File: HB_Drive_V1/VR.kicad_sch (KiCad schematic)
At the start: 0 parts

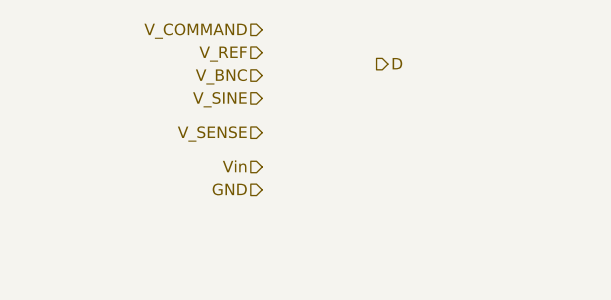
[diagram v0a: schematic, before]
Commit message: fixes git and adds a first revision of the Inner Current Regulator (NOT COMPLETE)
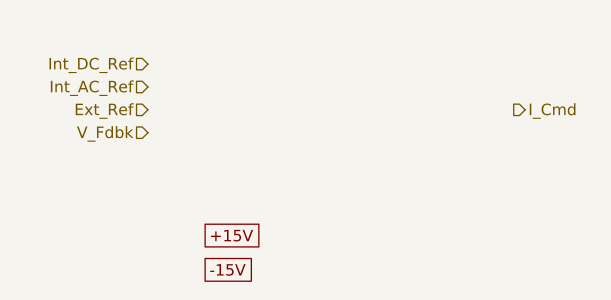
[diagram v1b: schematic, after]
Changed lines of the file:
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@@
 	(generator_version "10.0")
 	(paper "A4")
-	(hierarchical_label "V_REF"
+	(global_label "+15V"
+		(shape passive)
+		(at 120.65 86.36 0)
+		(fields_autoplaced yes)
+		(effects
+			(font
+				(size 1.27 1.27)
+			)
+			(justify left)
+		)
+		(property "Intersheetrefs" "${INTERSHEET_REFS}"
+			(at 127.6039 86.36 0)
+			(hide yes)
+			(show_name no)
+			(do_not_autoplace no)
+			(effects
+				(font
+					(size 1.27 1.27)
+				)
+				(justify left)
+			)
+		)
+	)
+	(global_label "-15V"
+		(shape passive)
+		(at 120.65 90.17 0)
+		(fields_autoplaced yes)
+		(effects
+			(font
+				(size 1.27 1.27)
+			)
+			(justify left)
+		)
+		(property "Intersheetrefs" "${INTERSHEET_REFS}"
+			(at 127.6039 90.17 0)
+			(hide yes)
+			(show_name no)
+			(do_not_autoplace no)
+			(effects
+				(font
+					(size 1.27 1.27)
+				)
+				(justify left)
+			)
+		)
+	)
+	(hierarchical_label "Int_AC_Ref"
 		(shape input)
-		(at 127 66.04 180)
+		(at 114.3 69.85 180)
 		(effects
 			(font
@@
 		)
 	)
-	(hierarchical_label "Vin"
+	(hierarchical_label "I_Cmd"
+		(shape output)
+		(at 154.94 72.39 0)
+		(effects
+			(font
+				(size 1.27 1.27)
+			)
+			(justify left)
+		)
+	)
+	(hierarchical_label "Ext_Ref"
 		(shape input)
-		(at 127 78.74 180)
+		(at 114.3 72.39 180)
 		(effects
 			(font
@@
 		)
 	)
-	(hierarchical_label "V_SINE"
+	(hierarchical_label "V_Fdbk"
 		(shape input)
-		(at 127 71.12 180)
+		(at 114.3 74.93 180)
 		(effects
 			(font
@@
 		)
 	)
-	(hierarchical_label "D"
-		(shape output)
-		(at 139.7 67.31 0)
+	(hierarchical_label "Int_DC_Ref"
+		(shape input)
+		(at 114.3 67.31 180)
 		(effects
 			(font
-				(size 1.27 1.27)
-			)
-			(justify left)
-		)
-	)
-	(hierarchical_label "V_BNC"
-		(shape input)
-		(at 127 68.58 180)
-		(effects
-			(font
-				(size 1.27 1.27)
-			)
-			(justify right)
-		)
-	)
-	(hierarchical_label "V_SENSE"
-		(shape input)
-		(at 127 74.93 180)
-		(effects
-			(font
-				(size 1.27 1.27)
-			)
-			(justify right)
-		)
-	)
-	(hierarchical_label "V_COMMAND"
-		(shape input)
-		(at 127 63.5 180)
-		(effects
-			(font
-				(size 1.27 1.27)
-			)
-			(justify right)
-		)
-	)
-	(hierarchical_label "GND"
-		(shape input)
-		(at 127 81.28 180)
-		(effects
-			(font

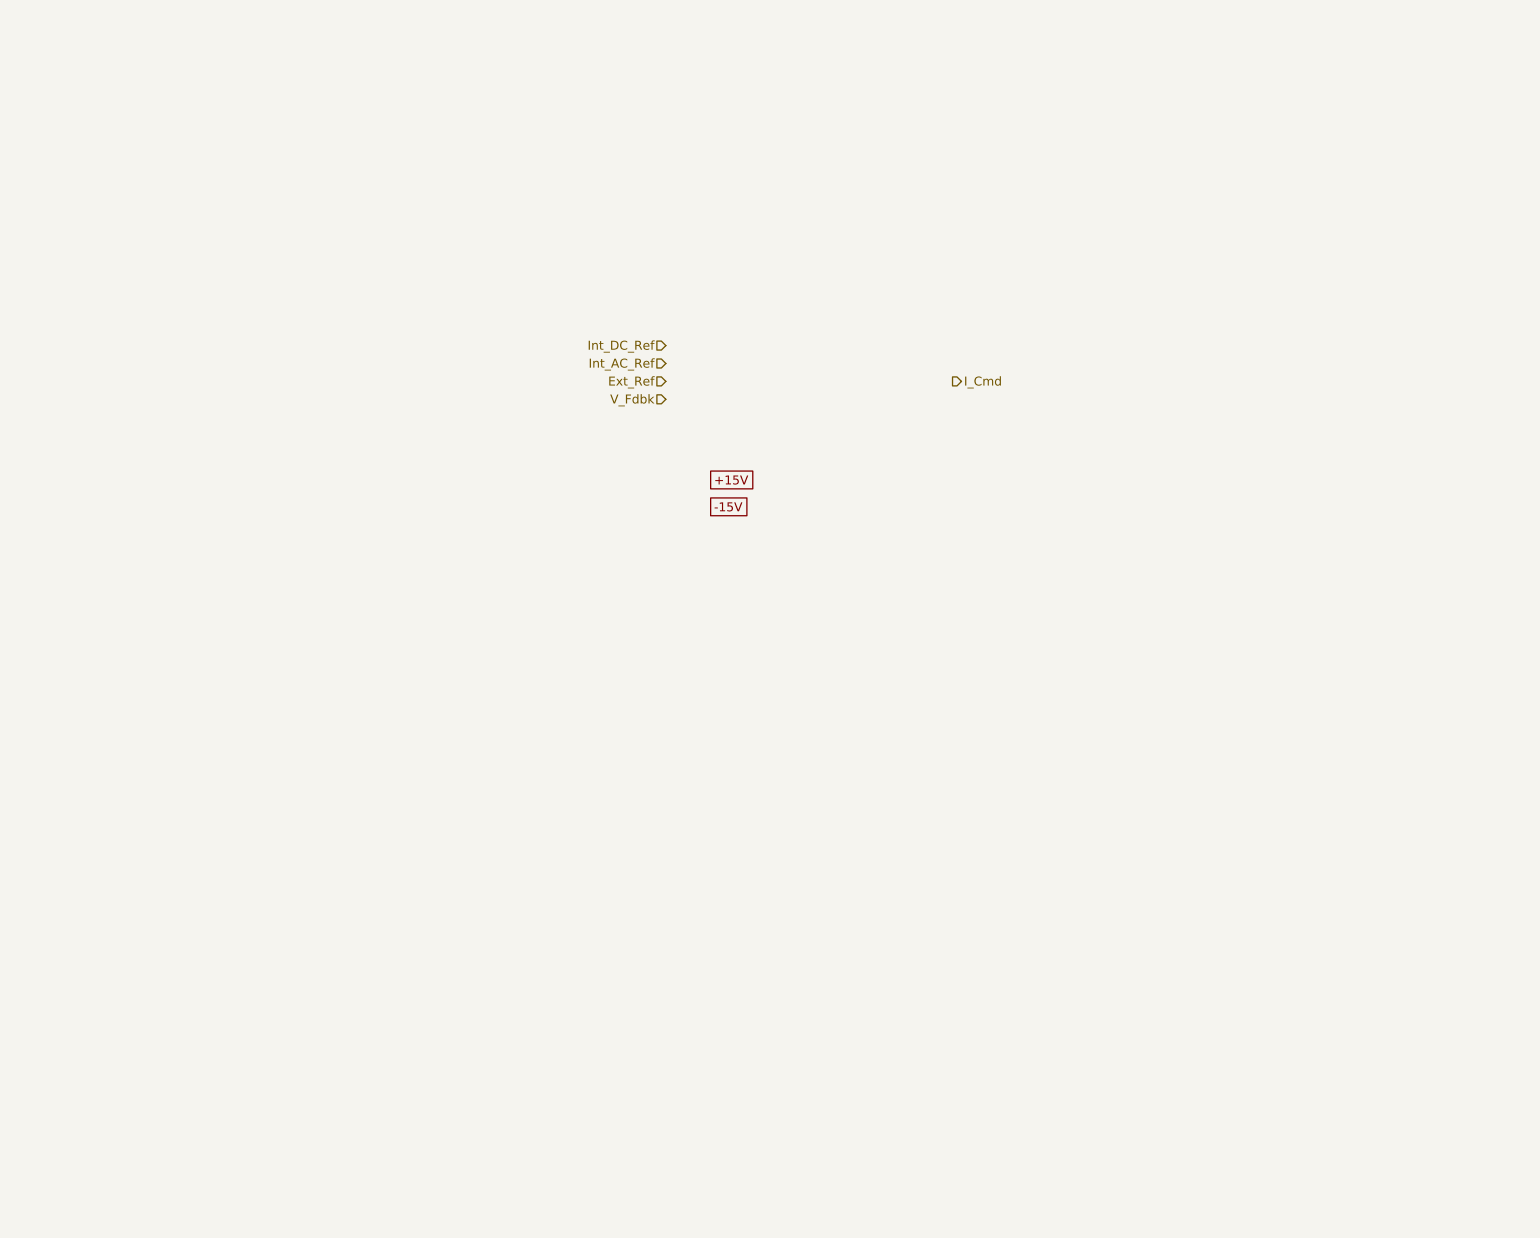
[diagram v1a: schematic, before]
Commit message: adds 10v reference and DC offsets / gain control to I_fdbk and V_fdbk
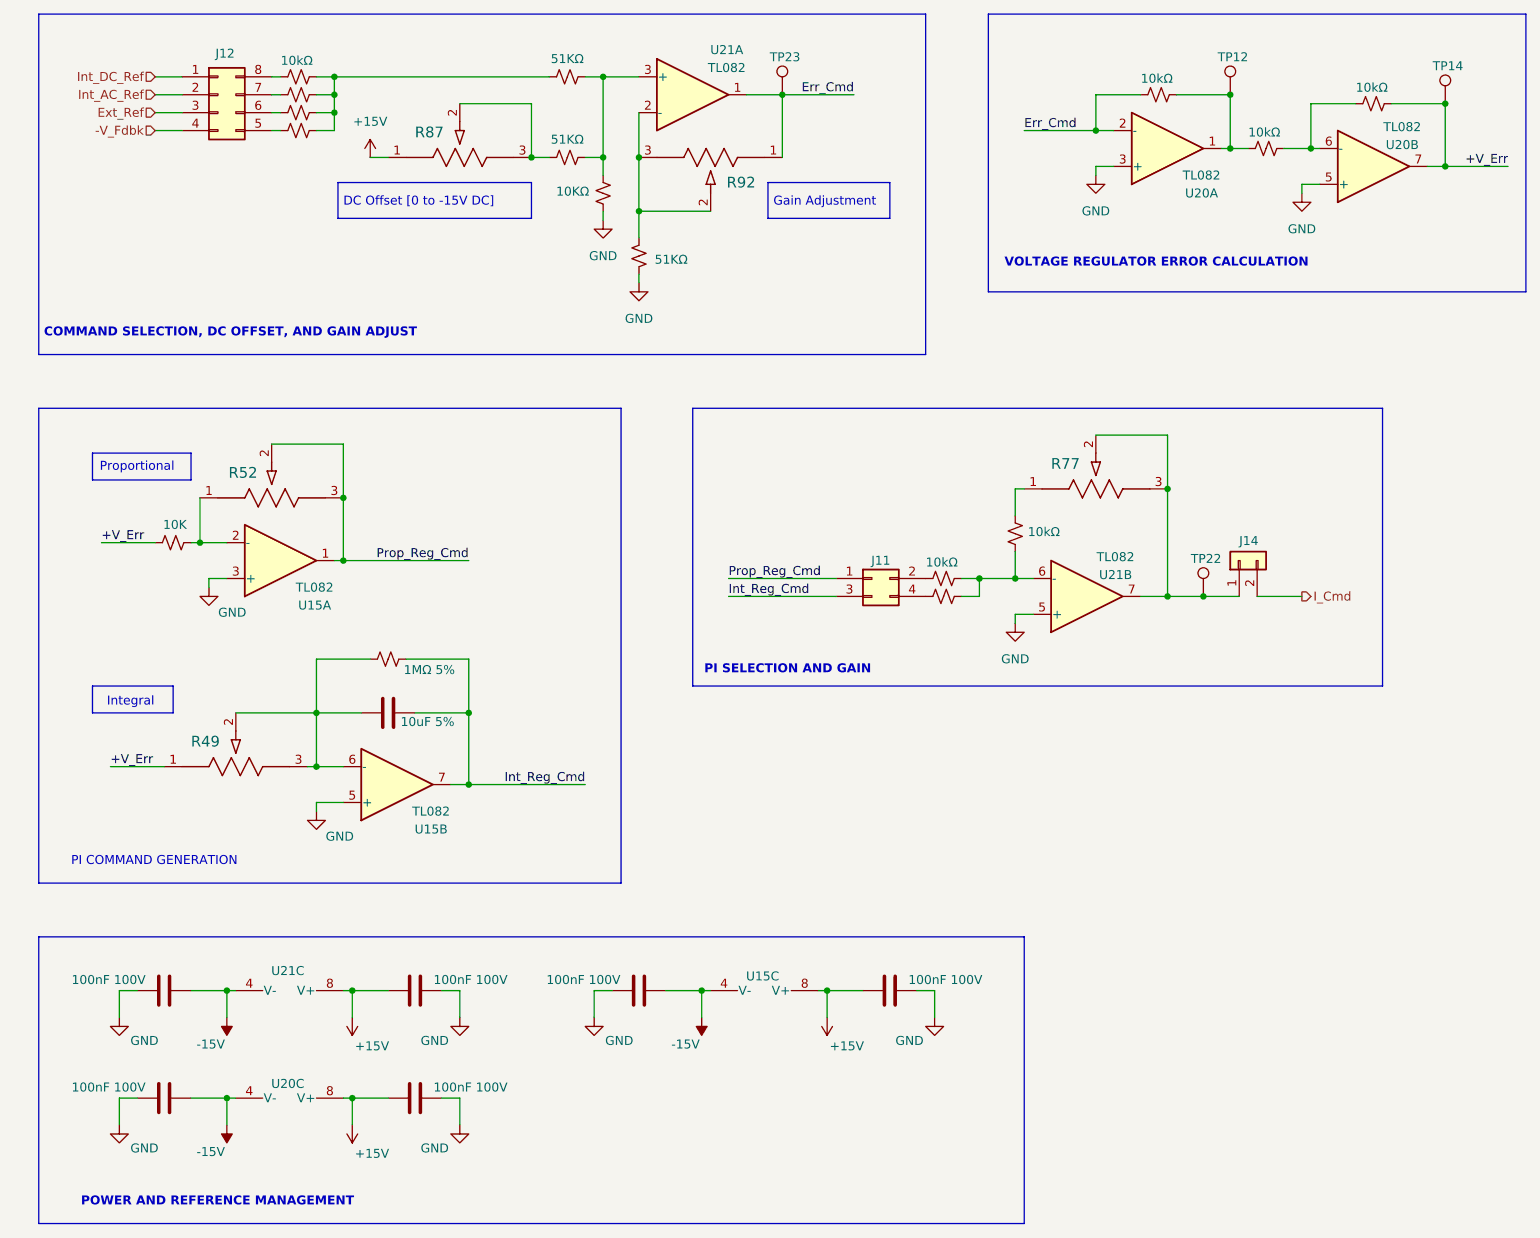
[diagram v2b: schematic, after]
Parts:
- added C27: 10uF 5%, Capacitor_SMD:C_0603_1608Metric, symbol Device:C
- added C43, C44, C45, C47, C48, C49: 100nF 100V, Capacitor_SMD:C_0603_1608Metric, symbol Device:C
- added J11: Conn_02x02_Odd_Even, Connector_PinSocket_1.27mm:PinSocket_2x02_P1.27mm_Vertical, symbol Connector_Generic:Conn_02x02_Odd_Even
- added J12: Conn_02x04_Counter_Clockwise, Connector_PinSocket_1.27mm:PinSocket_2x04_P1.27mm_Vertical, symbol Connector_Generic:Conn_02x04_Counter_Clockwise
- added J14: Conn_01x02, Connector_PinHeader_1.27mm:PinHeader_1x02_P1.27mm_Vertical, symbol Connector_Generic:Conn_01x02
- added R28, R59, R68, R69, R76, R82: 10kΩ, Resistor_SMD:R_0603_1608Metric_Pad0.98x0.95mm_HandSolder, symbol Device:R_Small_US
- added R29, R50, R83, R84, R85: 10K, Resistor_SMD:R_0603_1608Metric_Pad0.98x0.95mm_HandSolder, symbol Device:R_Small_US
- added R49, R52, R77, R87, R92: PV36W104C01B00, PV36W104C01B00:POT_PV36W_BRN, symbol PV36W104C01B00:PV36W104C01B00
- added R58: 1MΩ 5%, Resistor_SMD:R_0603_1608Metric_Pad0.98x0.95mm_HandSolder, symbol Device:R_Small_US
- added R88, R89, R91: 51KΩ, Resistor_SMD:R_0603_1608Metric_Pad0.98x0.95mm_HandSolder, symbol Device:R_Small_US
- added R90: 10KΩ, Resistor_SMD:R_0603_1608Metric_Pad0.98x0.95mm_HandSolder, symbol Device:R_Small_US
- added TP12, TP14, TP22, TP23: TestPoint, TestPoint:TestPoint_Loop_D2.60mm_Drill1.6mm_Beaded, symbol Connector:TestPoint
- added U15, U20: TL082, symbol Amplifier_Operational:TL082
- added U21: TL082, Package_SO:SOIC-8_5.3x5.3mm_P1.27mm, symbol Amplifier_Operational:TL082
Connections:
- net +15V: now also C47.2, C48.2, C49.2, R87.1, U15.8 (V+), U20.8 (V+), U21.8 (V+)
- net -15V: now also C43.1, C44.1, C45.1, U15.4 (V-), U20.4 (V-), U21.4 (V-)
- net Ext_Ref: now also J12.3 (Pin_3)
- net I_Cmd: now also J14.2 (Pin_2)
- net Int_AC_Ref: now also J12.2 (Pin_2)
- net Int_DC_Ref: now also J12.1 (Pin_1)
- new net: R50.2, R52.1, U15.2 (-)
- new net: J14.1 (Pin_1), R77.2, R77.3, TP22.1, U21.7
- new net: C27.2, R49.2, R49.3, R58.1, U15.6 (-)
- new net: R68.1, R69.2, U20.6 (-)
- new net: R76.2, R77.1
- new net: R88.1, R89.1, R90.2, U21.3 (+)
- new net: R59.1, R68.2, TP12.1, U20.1
- new net: J12.5 (Pin_5), R85.1
- new net: R82.1, R83.2, R84.2, R85.2, R88.2
- new net: R91.1, R92.2, R92.3, U21.2 (-)
- new net: J12.6 (Pin_6), R84.1
- new net: J12.7 (Pin_7), R83.1
- new net: J12.8 (Pin_8), R82.2
- new net: R87.2, R87.3, R89.2
- new net: J11.4 (Pin_4), R29.1
- new net: R28.1, R29.2, R76.1, U21.6 (-)
- new net: J11.2 (Pin_2), R28.2
- new net +V_Err: R49.1, R50.1, R69.1, TP14.1, U20.7
- new net -V_Fdbk: J12.4 (Pin_4)
- new net Err_Cmd: R59.2, R92.1, TP23.1, U20.2 (-), U21.1
- new net GND: C43.2, C44.2, C45.2, C47.1, C48.1, C49.1, R90.1, R91.2, U15.3 (+), U15.5 (+), U20.3 (+), U20.5 (+), U21.5 (+)
- new net Int_Reg_Cmd: C27.1, J11.3 (Pin_3), R58.2, U15.7
- new net Prop_Reg_Cmd: J11.1 (Pin_1), R52.2, R52.3, U15.1
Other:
- note added: "COMMAND SELECTION, DC OFFSET, AND GAIN ADJUST"
- note added: "DC Offset [0 to -15V DC]"
- note added: "Gain Adjustment"
- note added: "Integral"
- note added: "PI COMMAND GENERATION"
- note added: "PI SELECTION AND GAIN"
- note added: "POWER AND REFERENCE MANAGEMENT"
- note added: "Proportional"
- note added: "VOLTAGE REGULATOR ERROR CALCULATION"
